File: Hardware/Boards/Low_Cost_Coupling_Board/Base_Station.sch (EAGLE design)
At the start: 9 parts

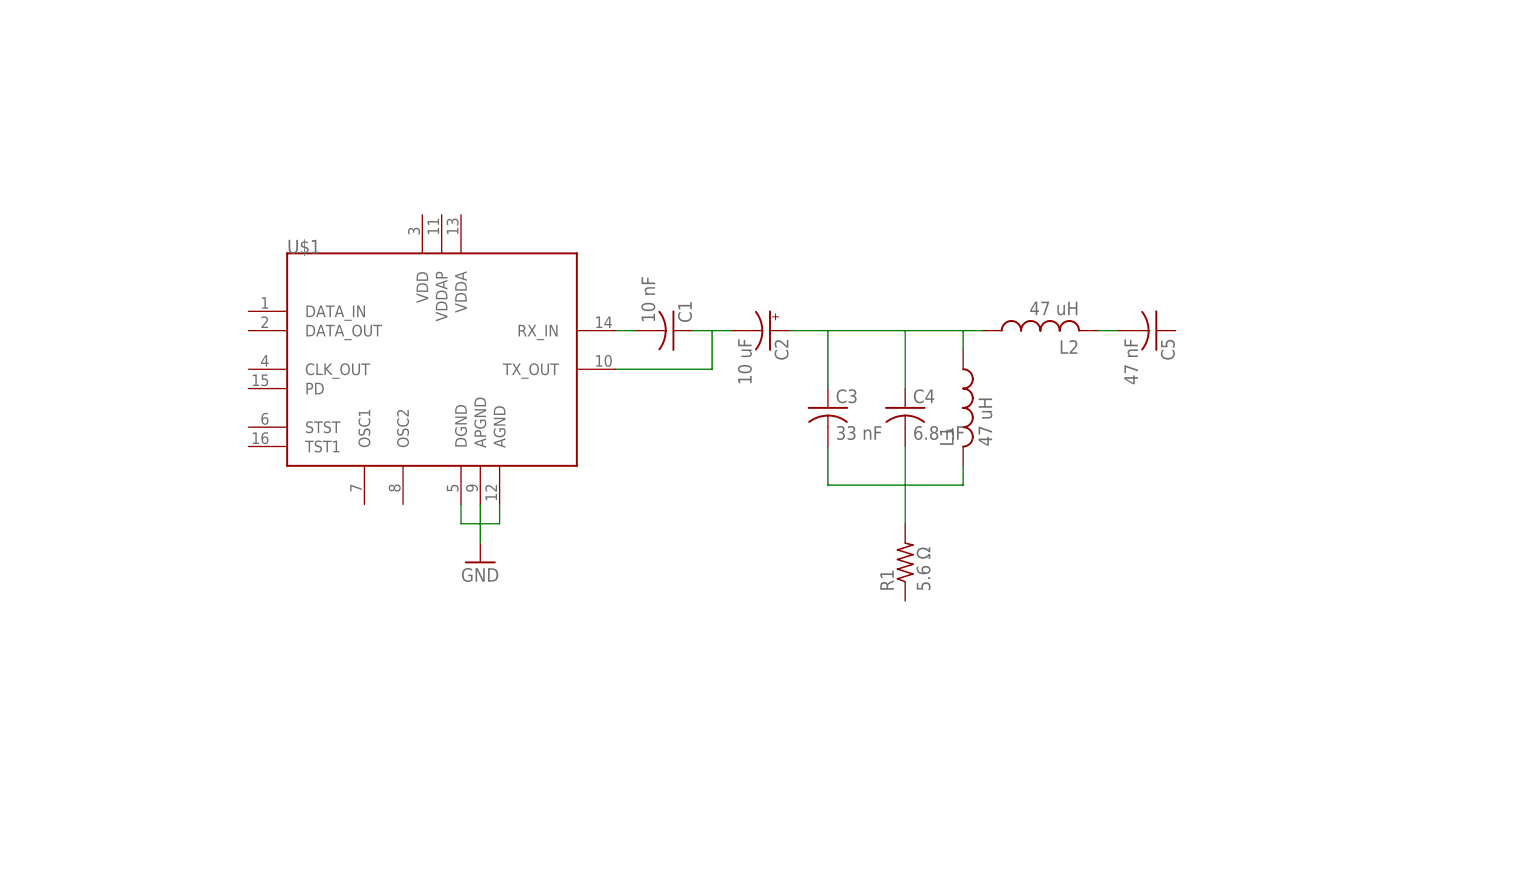
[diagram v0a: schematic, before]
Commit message: Finished schematic for low cost coupling board.
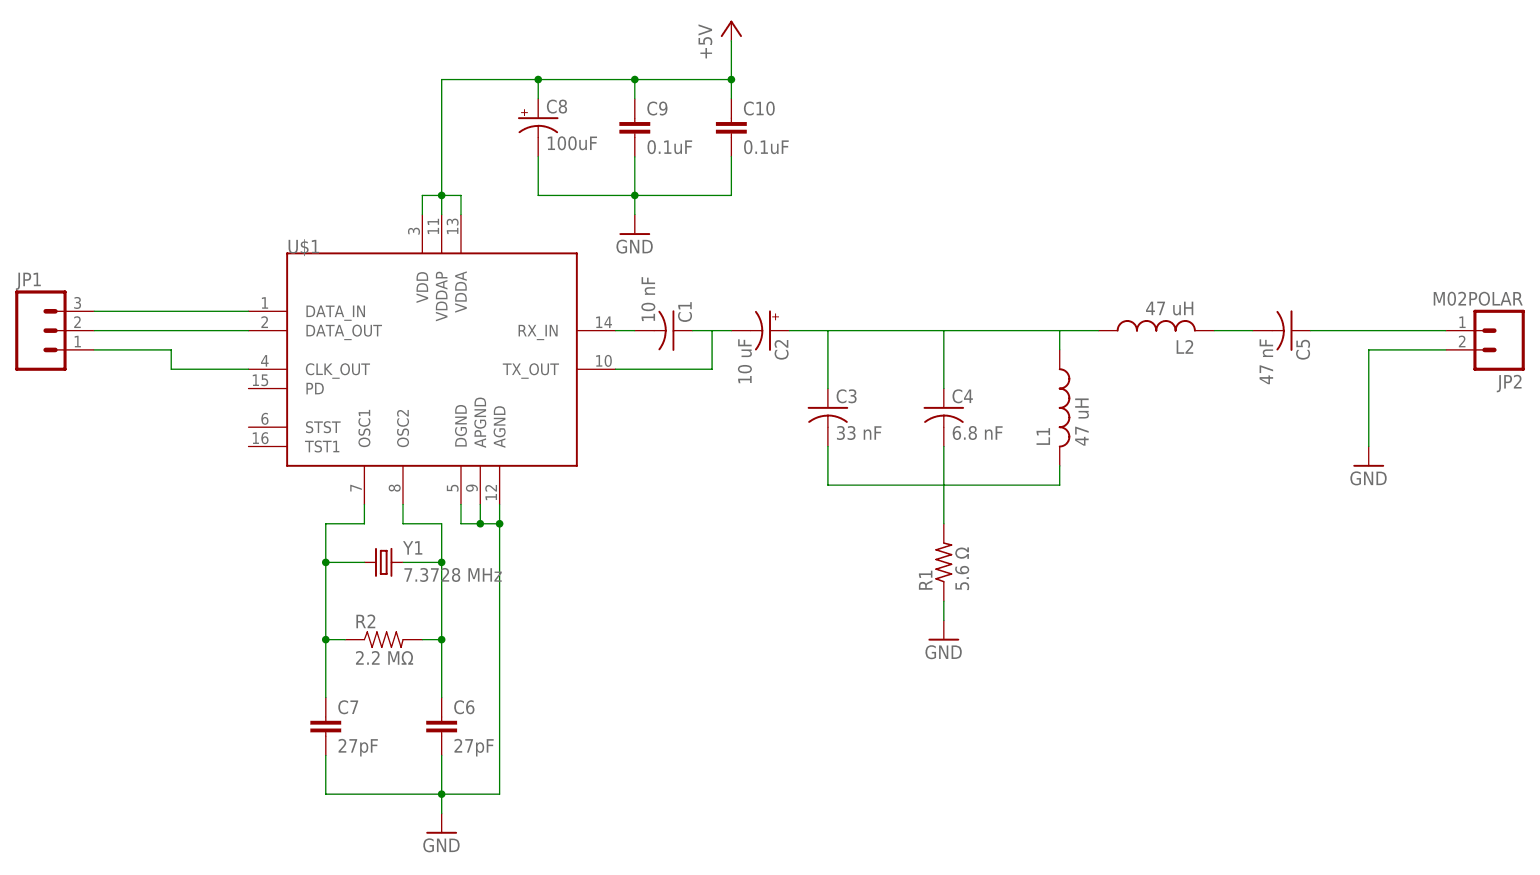
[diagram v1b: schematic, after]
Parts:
- added C10, C9: 0.1uF, SparkFun-Capacitors:CAPPTH1
- added C6, C7: 27pF, SparkFun-Passives:CAPPTH1
- added C8: 100uF, SparkFun-Capacitors:CAP_POLPTH1
- added JP1: (no value), SparkFun-Connectors:M03POLAR
- added JP2: M02POLAR, SparkFun-Connectors:M02POLAR
- added R2: 2.2 MΩ, SparkFun-Passives:RESISTORPTH-1/4W
- added Y1: 7.3728 MHz, SparkFun-FreqCtrl:CRYSTALHC49US
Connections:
- new net +5V: C10.1, C8.+, C9.1, U$1.VDD, U$1.VDDA, U$1.VDDAP
- new net N$10: JP1.2, U$1.DATA_OUT
- new net N$11: JP1.1, U$1.CLK_OUT
- new net N$6: C5.1, JP2.1
- new net N$7: C7.1, R2.1, U$1.OSC1, Y1.1
- new net N$8: C6.1, R2.2, U$1.OSC2, Y1.2
- new net N$9: JP1.3, U$1.DATA_IN
- net GND: now also C10.2, C6.2, C7.2, C8.-, C9.2, JP2.2, R1.1
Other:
- moved on the sheet: C4, C5, L1, L2, R1

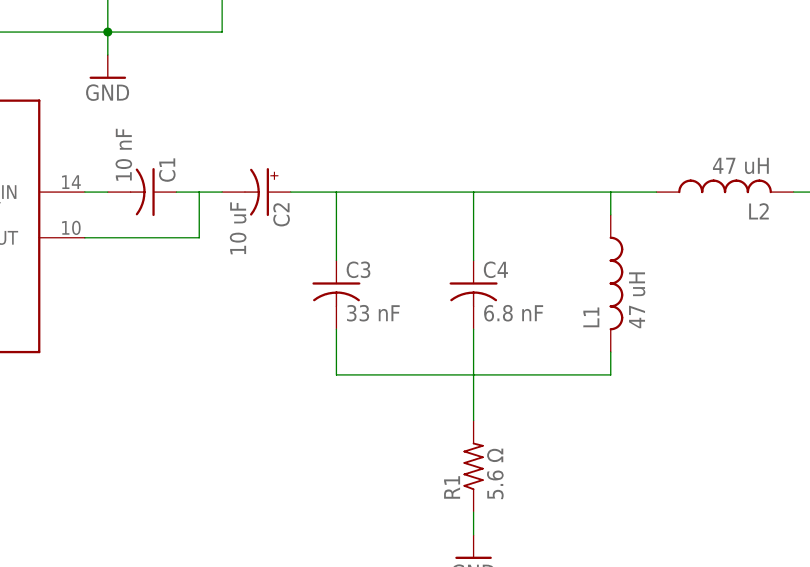
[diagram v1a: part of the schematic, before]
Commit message: Partially completed low cost coupling board
Decided it wasn't necessary tonight
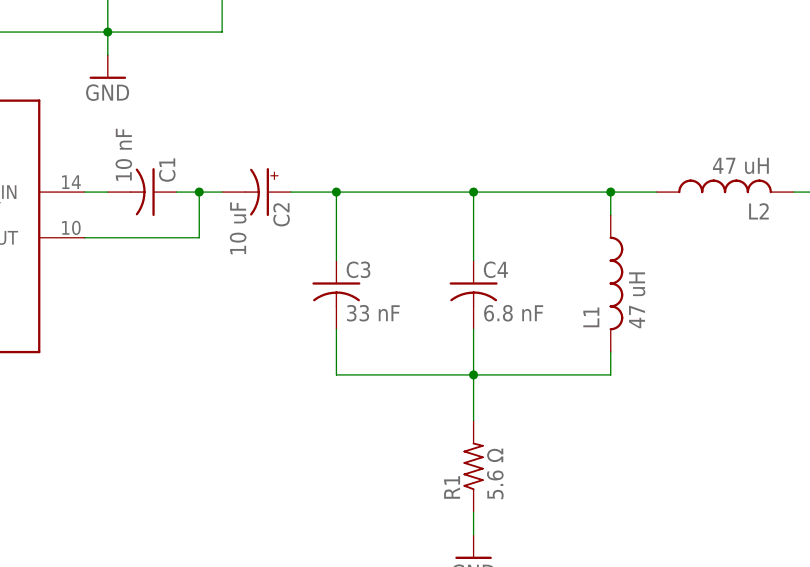
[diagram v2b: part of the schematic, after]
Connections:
- net N$3: now also C2.-
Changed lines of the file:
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@@
 <pinref part="C1" gate="G$1" pin="1"/>
 <wire x1="45.72" y1="78.74" x2="48.26" y2="78.74" width="0.1524" layer="91"/>
+<pinref part="C2" gate="G$1" pin="-"/>
+<junction x="48.26" y="78.74"/>
 </segment>
 </net>
@@
 <pinref part="L1" gate="G$1" pin="1"/>
 <wire x1="93.98" y1="76.2" x2="93.98" y2="78.74" width="0.1524" layer="91"/>
+<junction x="78.74" y="78.74"/>
+<junction x="63.5" y="78.74"/>
+<junction x="93.98" y="78.74"/>
 </segment>
 </net>
@@
 <wire x1="78.74" y1="58.42" x2="78.74" y2="53.34" width="0.1524" layer="91"/>
 <pinref part="R1" gate="G$1" pin="2"/>
+<junction x="78.74" y="58.42"/>
 </segment>
 </net>
@@
 </sheet>
 </sheets>
+<errors>
+</errors>
 </schematic>
 </drawing>
